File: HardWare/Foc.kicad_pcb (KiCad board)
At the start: 4 copper layers, 60 x 40 mm, 148 parts, among them J1 复用Typec, J2 hall, J3 Conn_01x03, J4 hall, J5 Conn_01x03, J6 SWD, J7 inp, J8 XH2.54, J9 SPI_conn, Q1 Q_NMOS_SGD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

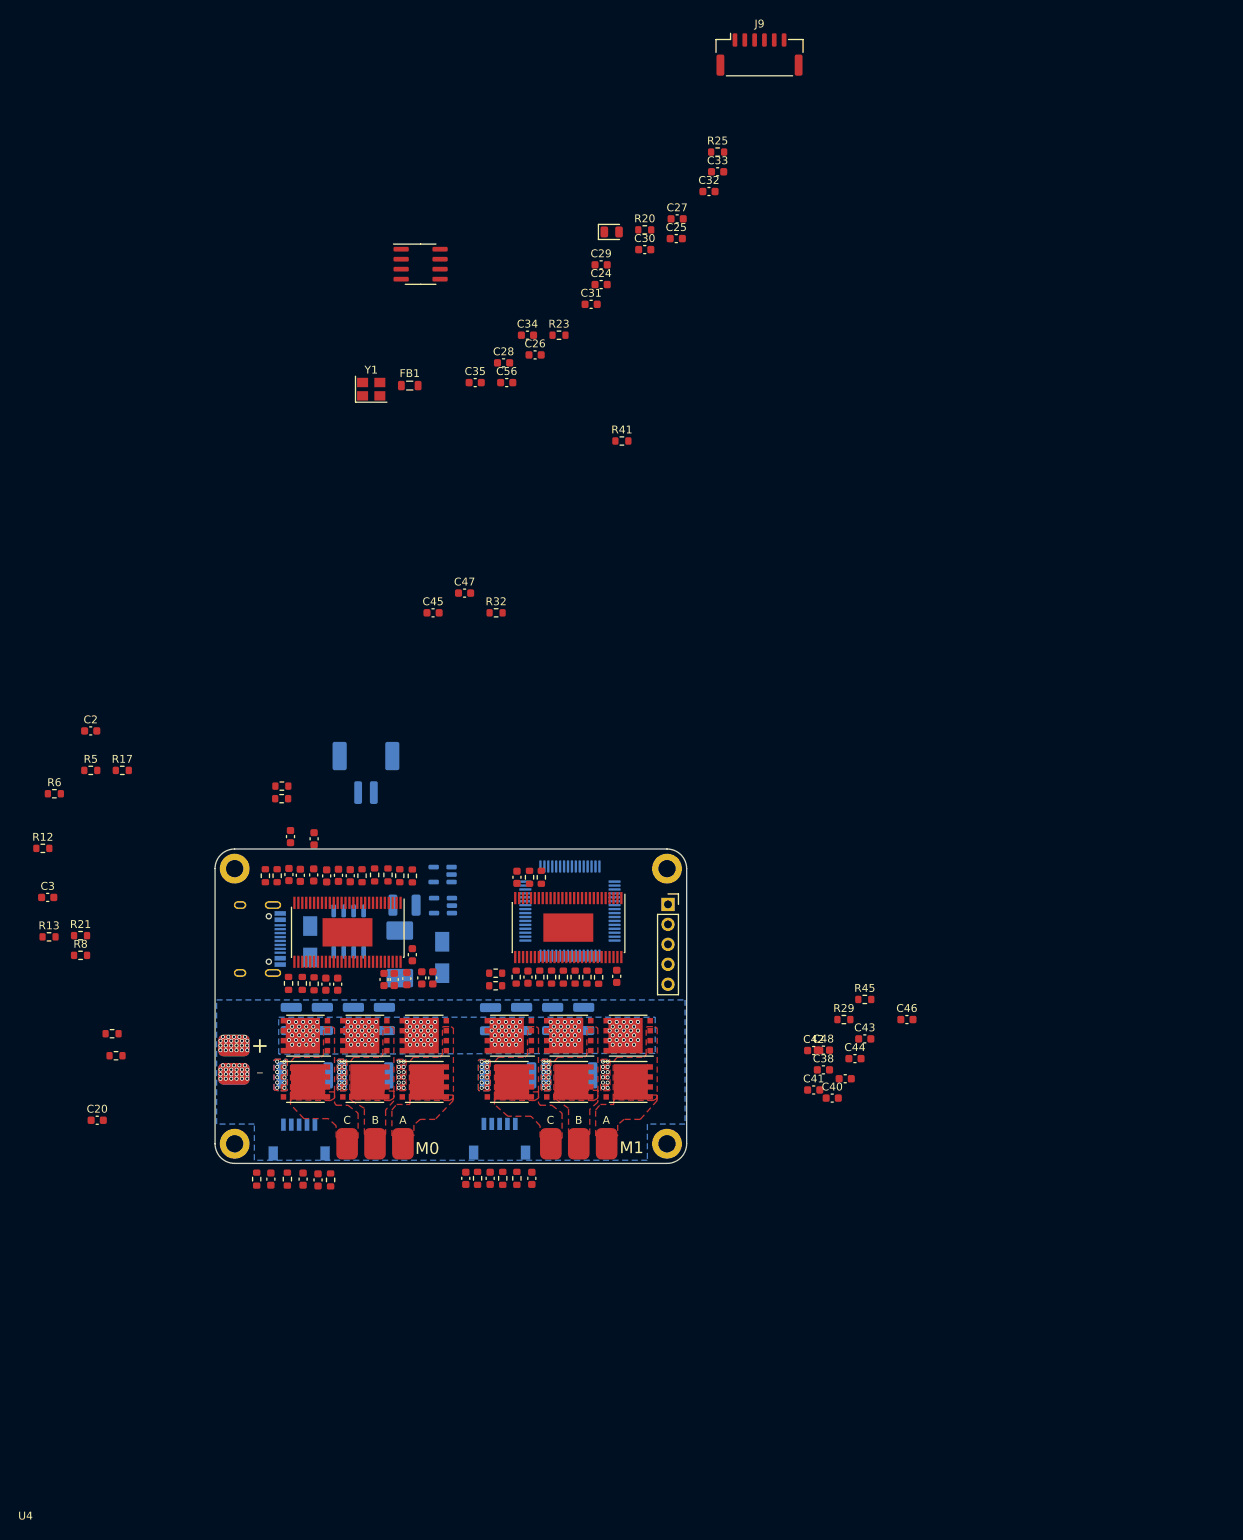
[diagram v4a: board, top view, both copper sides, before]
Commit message: 更新一些信号电源
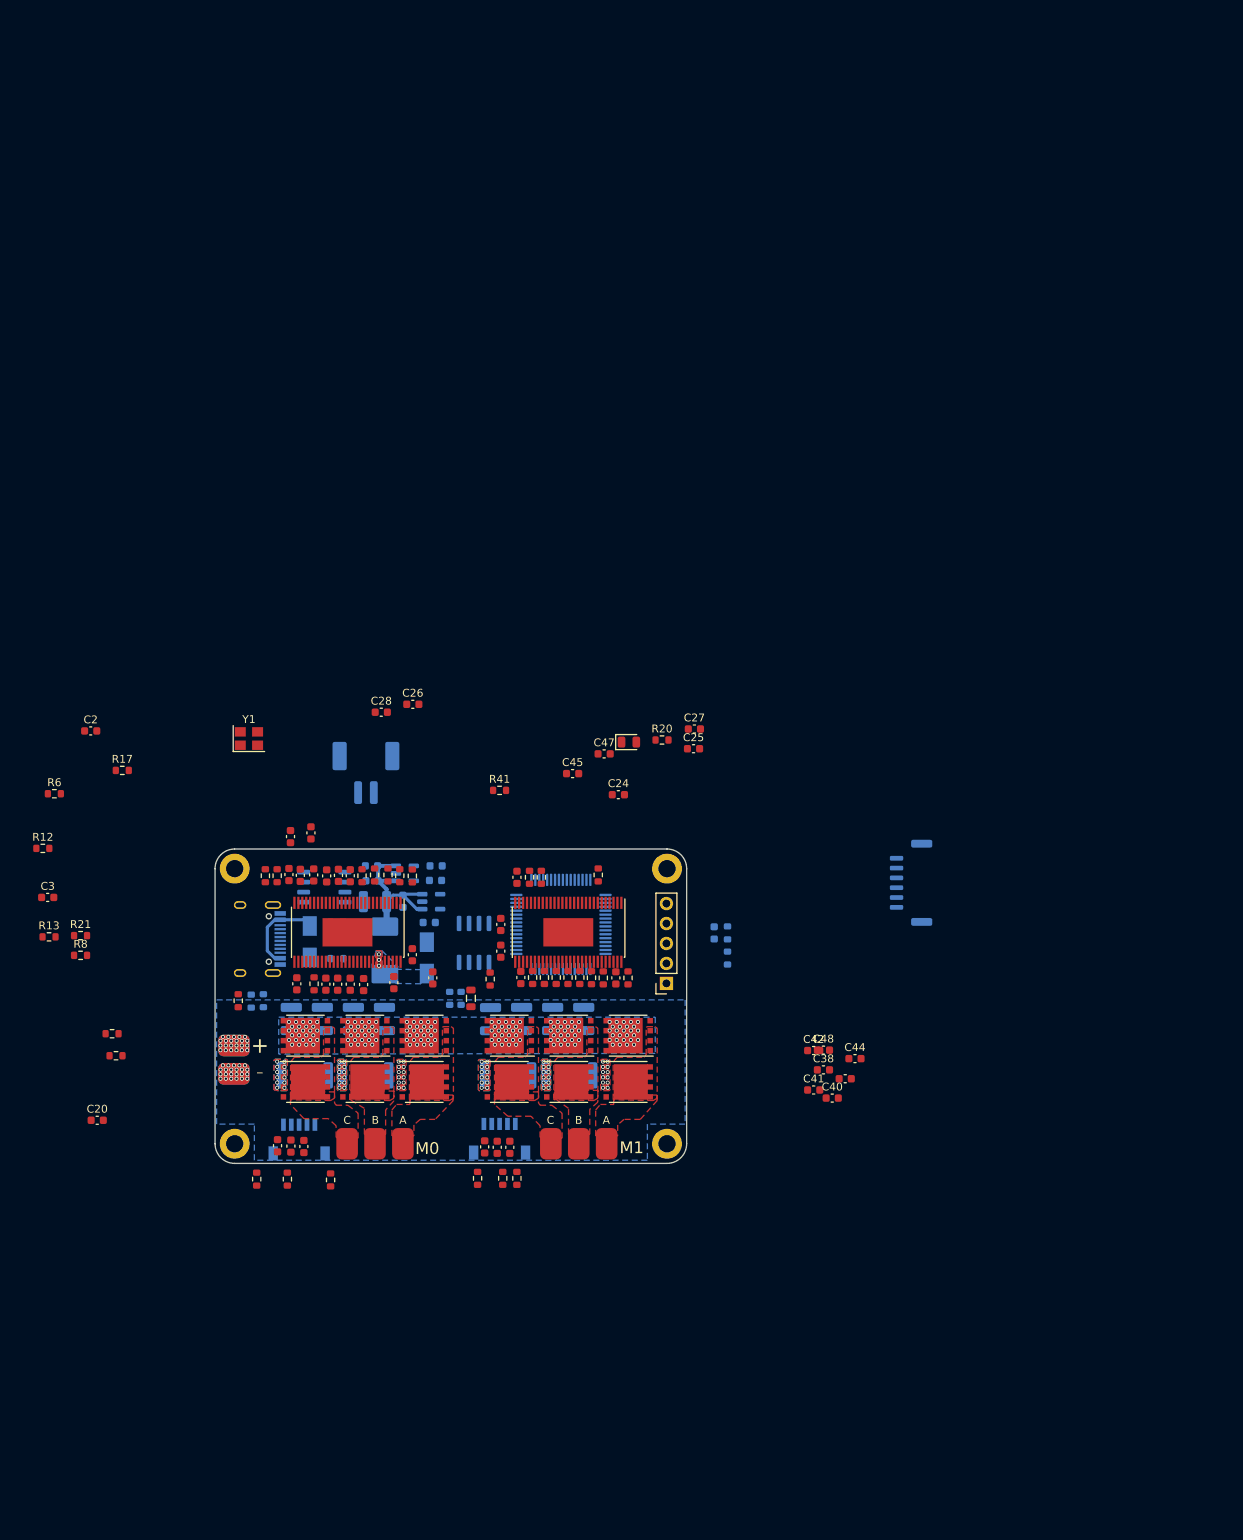
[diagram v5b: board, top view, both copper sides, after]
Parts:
- C29, C30, C31, C32, C33, C34, C35, C56, J9, R23, R25, R30, R32, R5, R50, R51, R7, U7: moved to B.Cu
- moved J9 107.1 mm to (143.6, 139.3), turned to -90 degrees
- moved C33 102.3 mm to (82.2, 144.3), turned to 180 degrees
- moved R25 99.3 mm to (120.2, 145.7), turned to 90 degrees
- moved C32 95.9 mm to (74.9, 137.2), turned to 180 degrees
- moved C30 87.5 mm to (75.0, 139.1), turned to 180 degrees
- moved U7 86.6 mm to (88.0, 146.9), turned to 90 degrees
- moved C29 86.2 mm to (118.5, 145.7), turned to 90 degrees
- moved R23 82.1 mm to (120.2, 148.9), turned to 90 degrees
- moved C31 79.6 mm to (78.9, 141.7), turned to -90 degrees
- moved FB1 78.3 mm to (87.5, 154.0), turned to 90 degrees
- moved C56 72.0 mm to (70.5, 144.3), turned to 180 degrees
- moved C34 68.5 mm to (83.1, 137.2)
- moved C24 64.9 mm to (106.3, 128.1)
- moved C25 64.9 mm to (115.9, 122.2)
- moved C27 64.9 mm to (116.0, 119.7)
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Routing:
- net +5V: track 0.00 -> 21.2 mm
- net Net-(D1-Pad1): track 0.00 -> 11.2 mm
- net /controller/SW_BST: vias 0 -> 3
- added copper zone on B.Cu, net /controller/SW_BST
- added copper zone on F.Cu, net /controller/SW_BST

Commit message: 日常更新
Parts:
- U1: moved to F.Cu
- moved U1 12.0 mm to (87.0, 144.9), turned to 180 degrees
- moved R45 4.31 mm to (94.3, 151.3)
- moved C13 3.85 mm to (79.0, 152.3)
- moved C42 3.27 mm to (132.4, 157.6)
- moved C12 2.71 mm to (65.9, 130.6)
- moved C9 2.71 mm to (63.3, 131.1)
- moved R29 2.09 mm to (105.7, 137.4)
- moved C39 2.09 mm to (95.3, 137.8)
- moved R34 2.09 mm to (96.9, 137.8)
- moved R35 2.09 mm to (98.4, 137.8)
- moved U5 2.09 mm to (101.8, 144.8)
- moved C49 1.91 mm to (107.9, 151.3)
- moved C36 1.91 mm to (95.8, 151.2)
- moved R31 1.91 mm to (97.3, 151.2)
- moved R33 1.91 mm to (98.8, 151.2)
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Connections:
- C35 pad 1: +3V3 -> +3.3V
- C56 pad 1: +3V3 -> +3.3V
- J6 pad 5: +3V3 -> +3.3V
- J9 pad 1: +3V3 -> +3.3V
- R20 pad 1: +3V3 -> +3.3V
- U1 pad 1: +3V3 -> +3.3V
- U1 pad 13: +3V3 -> +3.3V
- U1 pad 19: +3V3 -> +3.3V
- U1 pad 32: +3V3 -> +3.3V
- U1 pad 48: +3V3 -> +3.3V
- U1 pad 64: +3V3 -> +3.3V
- U4 pad 5: +3V3 -> +3.3V
- U6 pad 5: +3V3 -> +3.3V
- U6 pad 8: +3V3 -> +3.3V
- U7 pad 3: +3V3 -> +3.3V
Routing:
- net +3.3V: track 0.00 -> 2.16 mm, vias 0 -> 3
- net Net-(C34-Pad1): track 0.00 -> 2.06 mm
- net GND1: vias 47 -> 48
- added copper zone on In1.Cu, net +3.3V

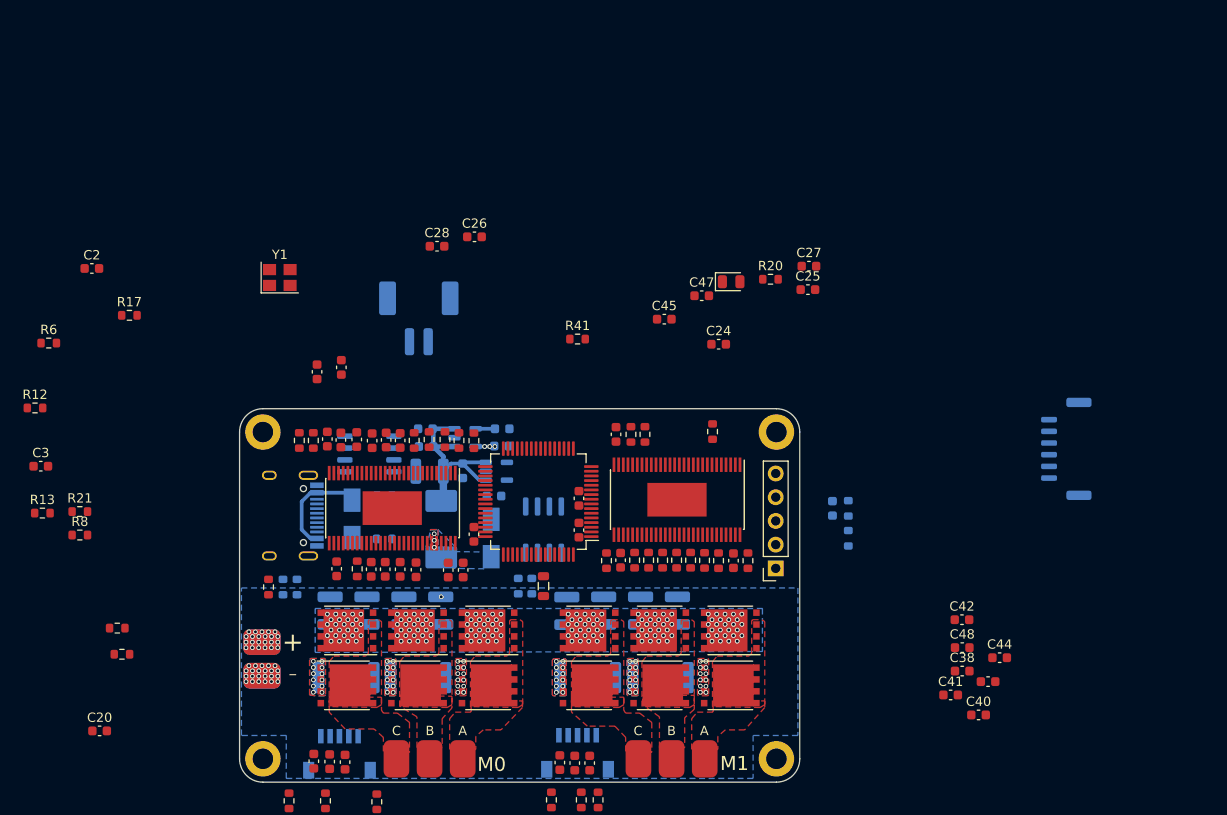
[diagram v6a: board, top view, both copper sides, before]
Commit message: 修改pcb中信号部分
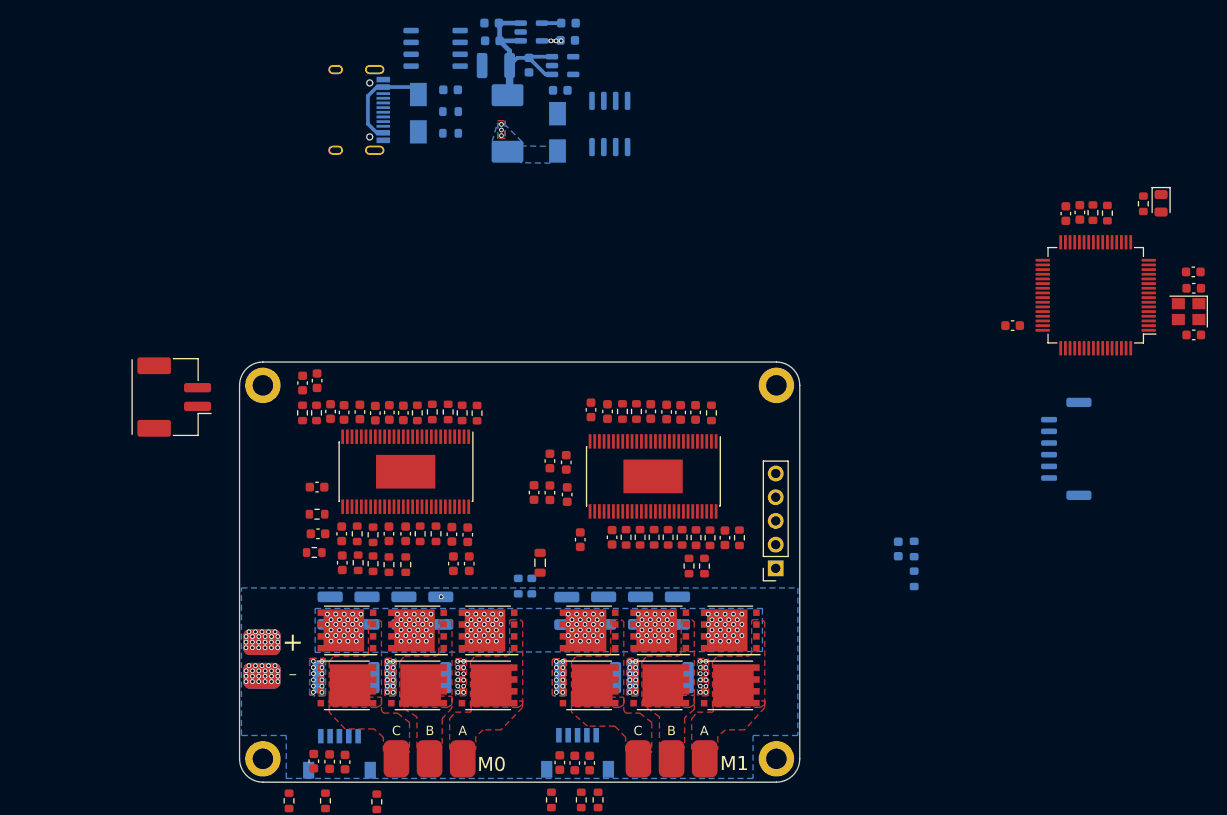
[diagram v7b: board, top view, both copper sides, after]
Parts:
- J8, R5, R7: moved to F.Cu
- moved C20 118.8 mm to (145.0, 114.0), turned to 90 degrees
- moved R15 115.6 mm to (147.9, 114.0), turned to 90 degrees
- moved R16 113.6 mm to (146.4, 114.0), turned to 90 degrees
- moved Y1 97.4 mm to (156.7, 124.6), turned to 180 degrees
- moved C28 81.0 mm to (157.2, 120.3), turned to 180 degrees
- moved U1 63.7 mm to (146.7, 122.8)
- moved C26 63.4 mm to (143.5, 114.1), turned to 90 degrees
- moved C40 52.8 mm to (92.6, 135.1), turned to -90 degrees
- moved C24 50.9 mm to (157.2, 127.1)
- moved D3 46.8 mm to (153.7, 113.0), turned to -90 degrees
- moved C37 46.3 mm to (91.5, 149.0), turned to 90 degrees
- moved C48 45.4 mm to (90.1, 144.2), turned to 90 degrees
- moved R12 45.0 mm to (76.0, 148.4), turned to -90 degrees
- moved C44 44.3 mm to (100.7, 135.3), turned to 90 degrees
- moved C30 44.0 mm to (82.1, 95.6)
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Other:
- board size 60 x 40 mm -> 60 x 45 mm

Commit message: 画一部分的信号
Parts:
- removed R39: R_Trim, Resistor_SMD:R_0603_1608Metric
- C20, C24, C25, C26, C27, C28, C7, D3, FB1, R15, R16, R20, U1, Y1: moved to B.Cu
- C56, R30, R32, U6: moved to F.Cu
- moved C20 62.2 mm to (94.1, 149.7), turned to -90 degrees
- moved R16 62.1 mm to (95.5, 149.7), turned to -90 degrees
- moved R15 62.1 mm to (97.0, 149.6), turned to -90 degrees
- moved C26 62.0 mm to (92.6, 149.6), turned to -90 degrees
- moved U7 56.5 mm to (59.9, 149.0), turned to 0 degrees
- moved C28 55.8 mm to (106.2, 143.3)
- moved C25 54.5 mm to (106.3, 141.6)
- moved U1 54.0 mm to (95.8, 140.8)
- moved Y1 52.9 mm to (105.8, 139.1)
- moved U3 52.5 mm to (70.0, 146.9), turned to -90 degrees
- moved C27 52.2 mm to (86.9, 137.6)
- moved C24 51.8 mm to (106.3, 136.6)
- moved C33 50.8 mm to (67.3, 146.7), turned to 90 degrees
- moved C35 50.4 mm to (73.8, 143.2)
- moved C31 50.0 mm to (72.6, 146.4)
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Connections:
- C43 pad 2: /motor2/M1_SH_C -> /motor2/M2_SH_C
- C47 pad 2: /motor2/M1_SH_B -> /motor2/M2_SH_B
- C48 pad 2: /motor2/M1_SH_A -> /motor2/M2_SH_A
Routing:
- net VDC: track 0.00 -> 33.1 mm
- net Net-(Q6-Pad2): track 0.00 -> 29.0 mm, vias 0 -> 2
- net Net-(Q4-Pad2): track 0.00 -> 22.8 mm
- net /motor2/M2_SL_B: track 0.00 -> 21.9 mm, vias 12 -> 14
- net Net-(Q2-Pad2): track 0.00 -> 18.5 mm
- net +5V: track 21.2 -> 3.70 mm
- net Net-(Q1-Pad2): track 0.00 -> 14.6 mm
- net /controller/M1_SL_B: track 0.00 -> 13.1 mm
- net /controller/SP1: track 0.00 -> 11.8 mm
- net /controller/SN1: track 0.00 -> 10.8 mm, vias 0 -> 2
- net /controller/M1_SH_A: track 0.00 -> 10.2 mm, vias 0 -> 2
- net /controller/SN2: track 0.00 -> 9.59 mm, vias 0 -> 2
- net Net-(C47-Pad1): track 0.00 -> 9.04 mm
- net /controller/M1_GH_A: track 0.00 -> 8.19 mm, vias 0 -> 2
- net /controller/M1_GL_C: track 0.00 -> 7.84 mm, vias 0 -> 2
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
